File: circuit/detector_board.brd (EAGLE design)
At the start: 60 x 60 mm, 16 parts

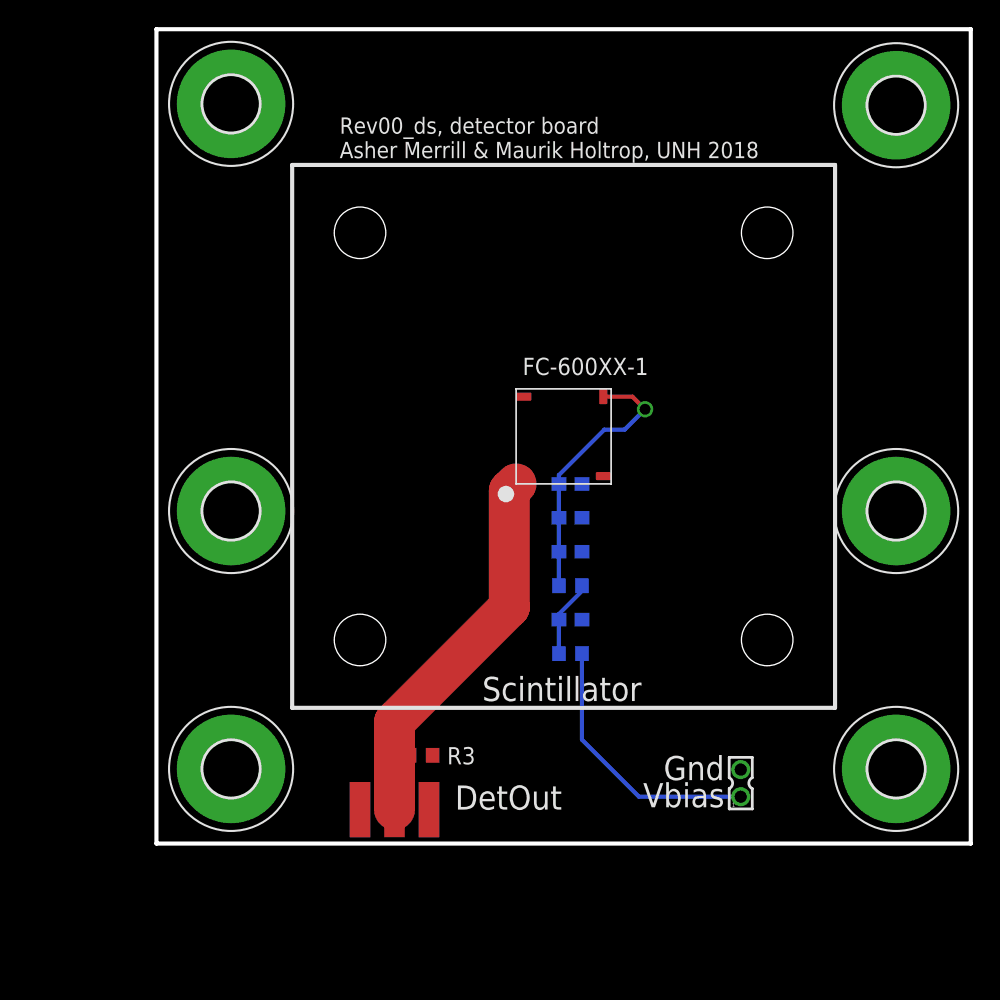
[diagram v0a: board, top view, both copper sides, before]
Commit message: Modified board. Tried to add Spice model.
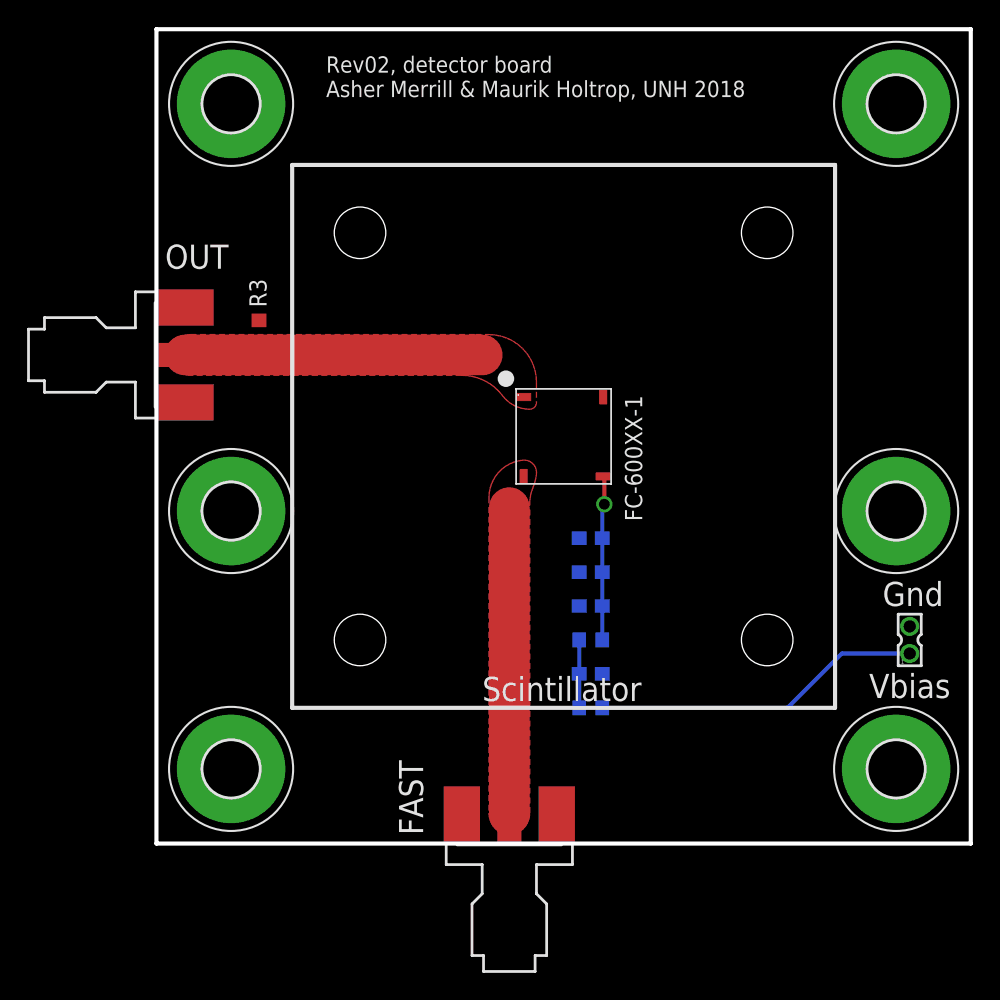
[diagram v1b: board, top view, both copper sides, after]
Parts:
- removed J$1: SMA_EDGE, SparkFun-Retired:SMA-EDGE
- added FAST, OUT: SMA-EDGE, 000phys605parts:SMA-EDGE
- FC-600XX-1: value FC-600XXBLANK -> SiPM; device 000phys605parts:FC-600XX-SMT_BLANK5 -> 000phys605parts:FC-600XX-SMT_FULL
- moved R3 33.4 mm to (7.55, 37.7), turned to 270 degrees
- moved SRC 16.3 mm to (55.5, 15.0)
- moved C3 6.67 mm to (32.0, 20.0), turned to 0 degrees
- moved C1 4.27 mm to (32.0, 12.5)
- moved C2 4.27 mm to (32.0, 17.5), turned to 0 degrees
- moved R1 4.27 mm to (32.0, 10.0)
- moved R2 4.27 mm to (32.0, 15.0), turned to 180 degrees
- moved C4 2.12 mm to (32.0, 22.5), turned to 0 degrees
- moved H4 0.10 mm to (54.5, 54.5)
- turned FC-600XX-1 to 270 degrees
- turned H1 to 90 degrees
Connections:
- net N$1 renamed P1
- net N$4 renamed IN
- removed net V_AN: FC-600XX-1.P_AN, J$1.SIG, R3.2
- new net FAST: FAST.G@0, FC-600XX-1.F_FAST
- new net OUT: FC-600XX-1.P_AN, OUT.G@0, R3.2
- net GND: now also FAST.G@1, FAST.G@2, FAST.G@3, FAST.G@4, OUT.G@1, OUT.G@2, OUT.G@3, OUT.G@4; no longer J$1.GND@0, J$1.GND@1, J$1.GND@2, J$1.GND@3
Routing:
- net V_AN: track 29.9 -> 0.00 mm
- net FAST: track 0.00 -> 22.6 mm
- net OUT: track 0.00 -> 21.9 mm
- net VBIAS: track 20.0 -> 12.1 mm
- net IN: track 19.8 -> 24.3 mm
- net P1: track 5.70 -> 5.00 mm
- added copper zone on layer 1, net FAST
- added copper zone on layer 1, net OUT
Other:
- board text added: "Rev02, detector board Asher Merrill & Maurik Holtrop, UNH 2018"
- board text removed: "DetOut"
- board text removed: "Rev00_ds, detector board Asher Merrill & Maurik Holtrop, UNH 2018"

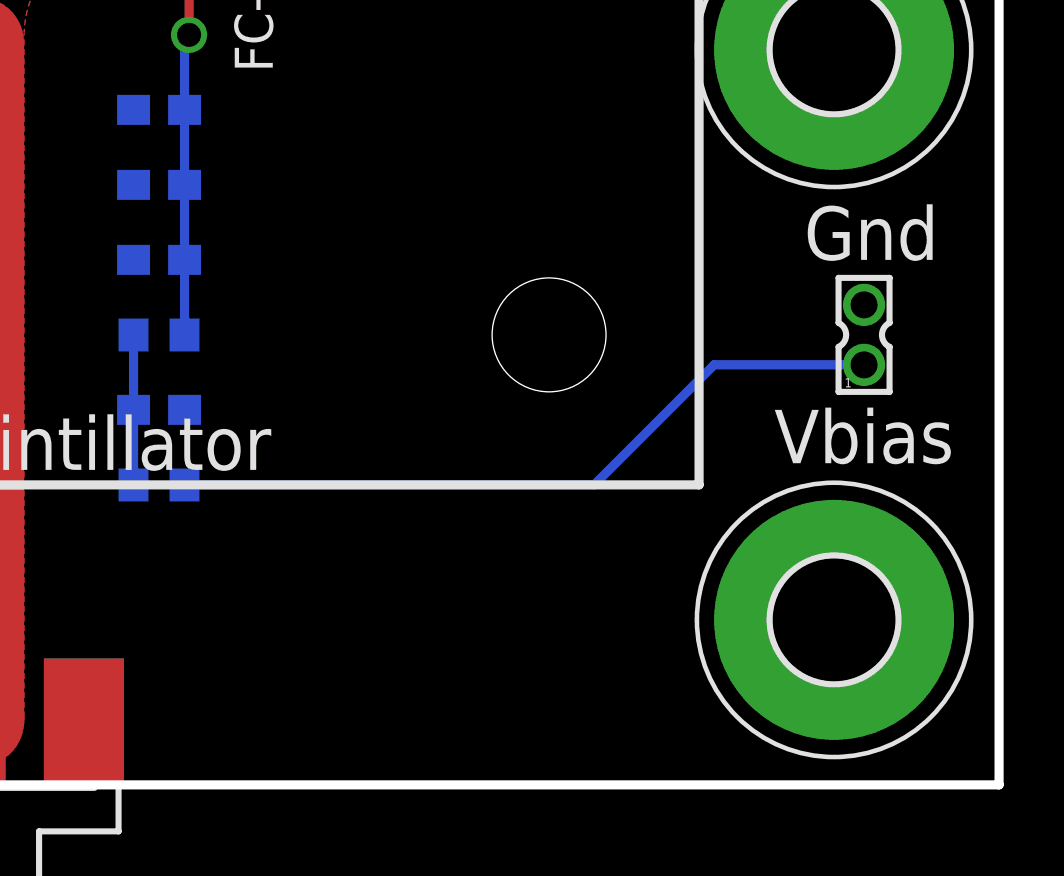
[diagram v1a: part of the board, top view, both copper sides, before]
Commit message: boards: Added VEE line to header.  Corrected header to be 0.100", (what we have in stock,) not 2mm header.
Also added filtering caps (backwards, sort of,) to stabilize the VEE line.
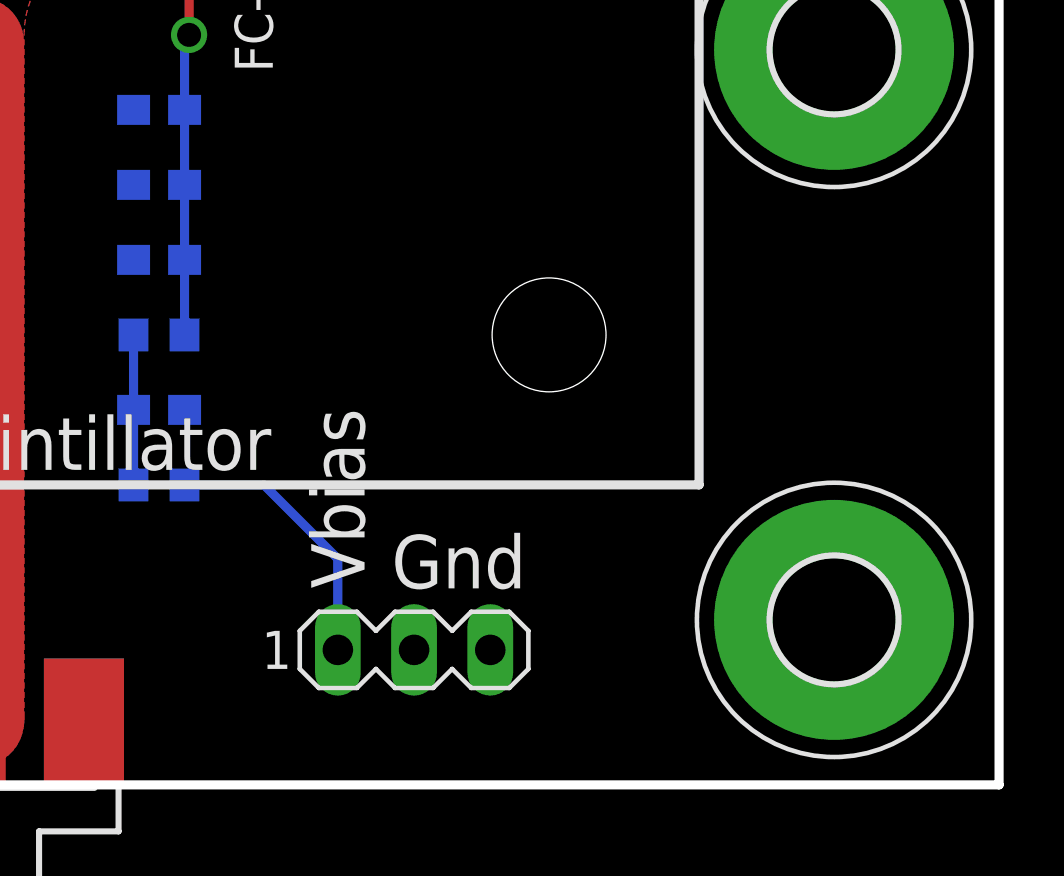
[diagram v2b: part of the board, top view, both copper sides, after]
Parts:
- removed SRC: (no value), con-garry:332-02
- added SV1: (no value), con-lstb:MA03-1
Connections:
- net GND: now also SV1.2, SV1.3; no longer SRC.2
- net IN: now also SV1.1; no longer SRC.1
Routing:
- net IN: track 24.3 -> 9.17 mm
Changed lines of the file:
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@@
 <hole x="15" y="45" drill="3.7973"/>
 <text x="24" y="10.5" size="1.778" layer="25">Scintillator</text>
-<text x="58.5" y="12.5" size="1.778" layer="21" rot="R180">Vbias</text>
-<text x="53.5" y="17.5" size="1.778" layer="21">Gnd</text>
+<text x="38.85" y="6.55" size="1.778" layer="21" rot="R90">Vbias</text>
+<text x="39.75" y="6.55" size="1.778" layer="21">Gnd</text>
 <text x="12.5" y="55" size="1.2" layer="21">Rev02, detector board
 Asher Merrill &amp; Maurik Holtrop, UNH 2018</text>
@@
 </autorouter>
 <elements>
-<element name="SRC" library="con-garry" library_urn="urn:adsk.eagle:library:147" package="332-02" package3d_urn="urn:adsk.eagle:package:6810/1" value="" x="55.5" y="15" smashed="yes">
-<attribute name="VALUE" x="54.88" y="17.54" size="1.27" layer="27"/>
-</element>
 <element name="OUT" library="000phys605parts" package="SMA-EDGE" value="SMA-EDGE" x="0" y="36">
 <attribute name="SPICEPREFIX" value="B" x="0" y="36" size="1.778" layer="27" display="off"/>
@@
 <element name="H5" library="holes" library_urn="urn:adsk.eagle:library:237" package="4,1-PAD" package3d_urn="urn:adsk.eagle:package:14285/1" value="MOUNT-PAD-ROUND4.1" x="5.5" y="24.5"/>
 <element name="H6" library="holes" library_urn="urn:adsk.eagle:library:237" package="4,1-PAD" package3d_urn="urn:adsk.eagle:package:14285/1" value="MOUNT-PAD-ROUND4.1" x="54.5" y="24.5"/>
+<element name="SV1" library="con-lstb" library_urn="urn:adsk.eagle:library:162" package="MA03-1" package3d_urn="urn:adsk.eagle:package:8339/1" value="" x="40.5" y="4.5" smashed="yes">
+<attribute name="MF" value="" x="40.5" y="4.5" size="1.778" layer="27" display="off"/>
+<attribute name="MPN" value="" x="40.5" y="4.5" size="1.778" layer="27" display="off"/>
+<attribute name="OC_FARNELL" value="unknown" x="40.5" y="4.5" size="1.778" layer="27" display="off"/>
+<attribute name="OC_NEWARK" value="unknown" x="40.5" y="4.5" size="1.778" layer="27" display="off"/>
+<attribute name="VALUE" x="36.69" y="1.579" size="1.27" layer="27" ratio="10"/>
+</element>
 </elements>
 <signals>
@@
 </signal>
 <signal name="GND">
-<contactref element="SRC" pad="2"/>
 <polygon width="0.184" layer="1" rank="6">
 <vertex x="0" y="60"/>
@@
 <contactref element="H6" pad="B4,1"/>
 <contactref element="H5" pad="B4,1"/>
+<contactref element="SV1" pad="2"/>
+<contactref element="SV1" pad="3"/>
 </signal>
 <signal name="OUT" class="1">
@@
 </signal>
 <signal name="IN">
-<contactref element="SRC" pad="1"/>
 <contactref element="R1" pad="1"/>
-<wire x1="32.85" y1="10" x2="46.5" y2="10" width="0.3048" layer="16"/>
-<wire x1="46.5" y1="10" x2="50.5" y2="14" width="0.3048" layer="16"/>
-<wire x1="50.5" y1="14" x2="55.5" y2="14" width="0.3048" layer="16"/>
+<contactref element="SV1" pad="1"/>
+<wire x1="32.85" y1="10" x2="35.5" y2="10" width="0.3048" layer="16"/>
+<wire x1="35.5" y1="10" x2="37.96" y2="7.54" width="0.3048" layer="16"/>
+<wire x1="37.96" y1="7.54" x2="37.96" y2="4.5" width="0.3048" layer="16"/>
 </signal>
 <signal name="FAST" class="1">
